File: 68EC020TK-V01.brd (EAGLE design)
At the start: 124.9 x 100 mm, 100 parts, among them IC10 74HCT245PW, IC11 74HCT245PW, IC12 AM29F010S, IC13 XC95288XL-TQ144, IC14 ICS570B, IC15 74HCT245PW, IC2 MC68EC020RP, IC3 74ACT16245, IC4 74ACT16245, IC5 LD117AS33TR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

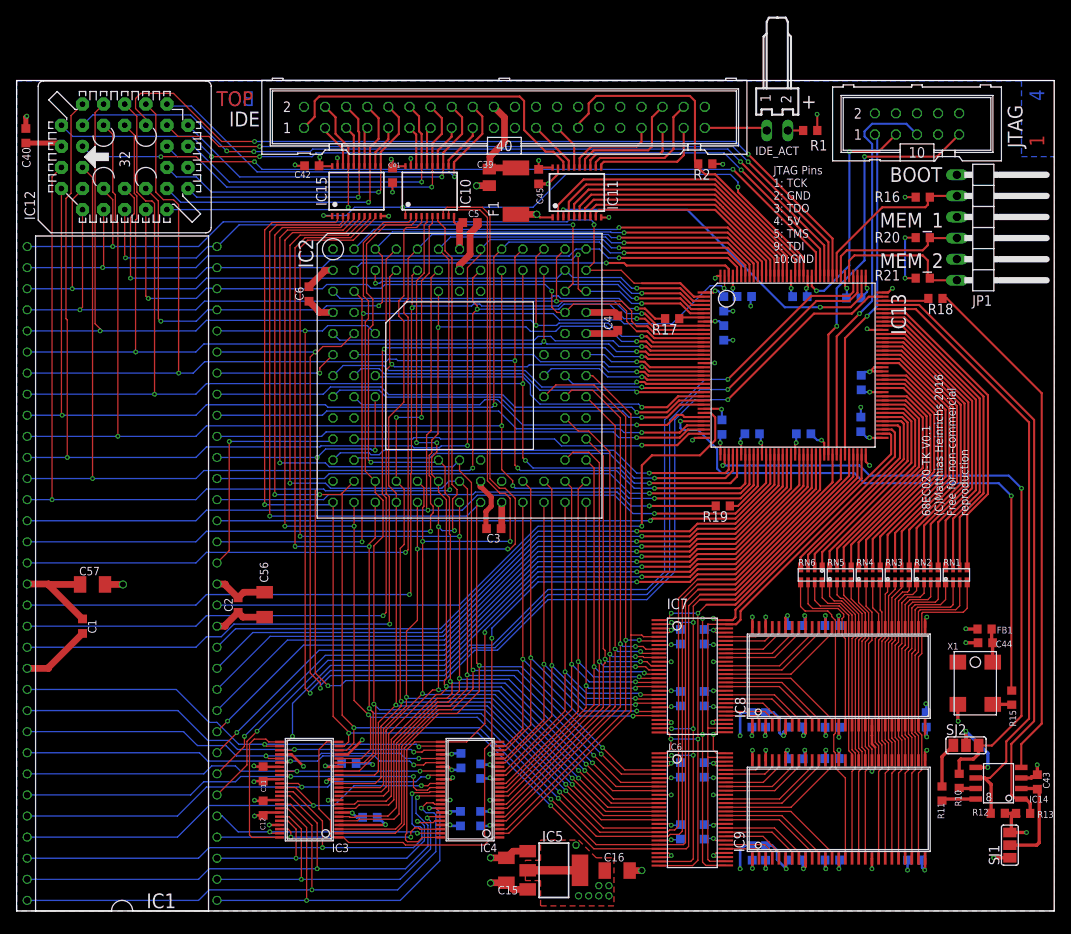
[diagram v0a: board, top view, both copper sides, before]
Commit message: bus & autoconfig OK IDE-RW-fix but IDE& mem not working
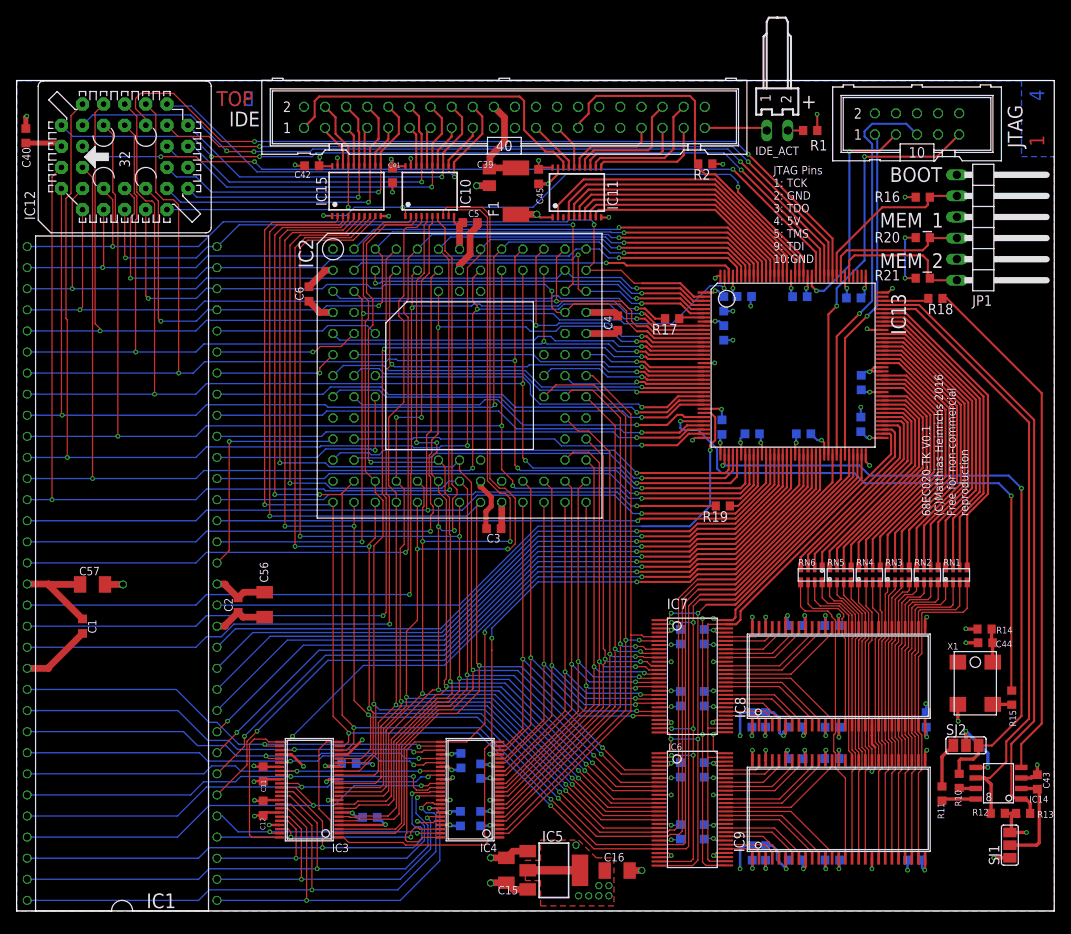
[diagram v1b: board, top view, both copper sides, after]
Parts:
- R14: value 100Ohm@100MHz -> (none)
- renumbered FB1 to R14
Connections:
- net !BERR: no longer IC13.107
- net C_IDE_W: no longer IC13.110
- net FC0: no longer IC13.112
- net FC1: no longer IC13.111
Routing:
- net FC0: track 161.8 -> 19.7 mm, vias 3 -> 0
- net FC1: track 156.0 -> 17.4 mm, vias 3 -> 1
- net !BERR: track 151.1 -> 26.0 mm, vias 4 -> 1
- net C_IDE_W: track 44.7 -> 0.00 mm, vias 2 -> 0
- net ABUS_U: track 101.8 -> 99.5 mm
